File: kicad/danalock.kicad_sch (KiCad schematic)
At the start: 10 parts, among them J1 Conn_02x02_Top_Bottom, M1 Motor_DC, SW1 Rotary_Encoder, U1 WeMos_D1_mini, U2 HW-133, U3 TB6612FNG_Module

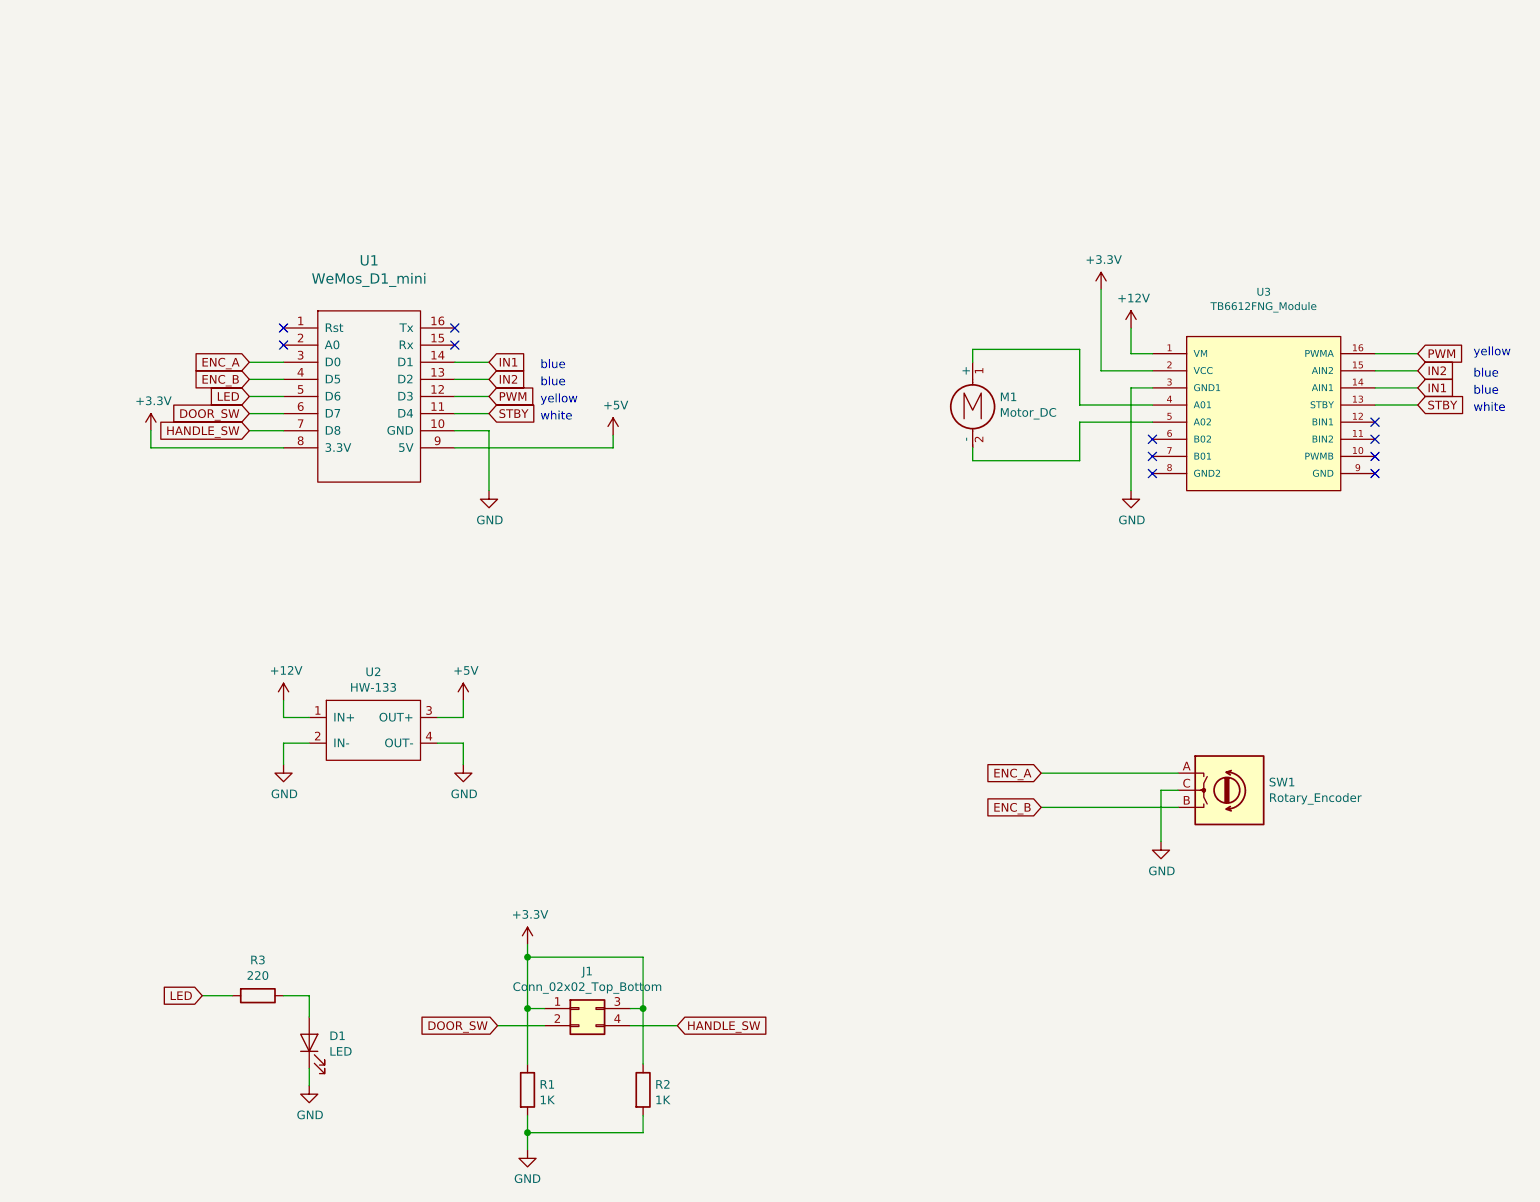
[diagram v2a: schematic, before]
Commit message: Port to ESP32.
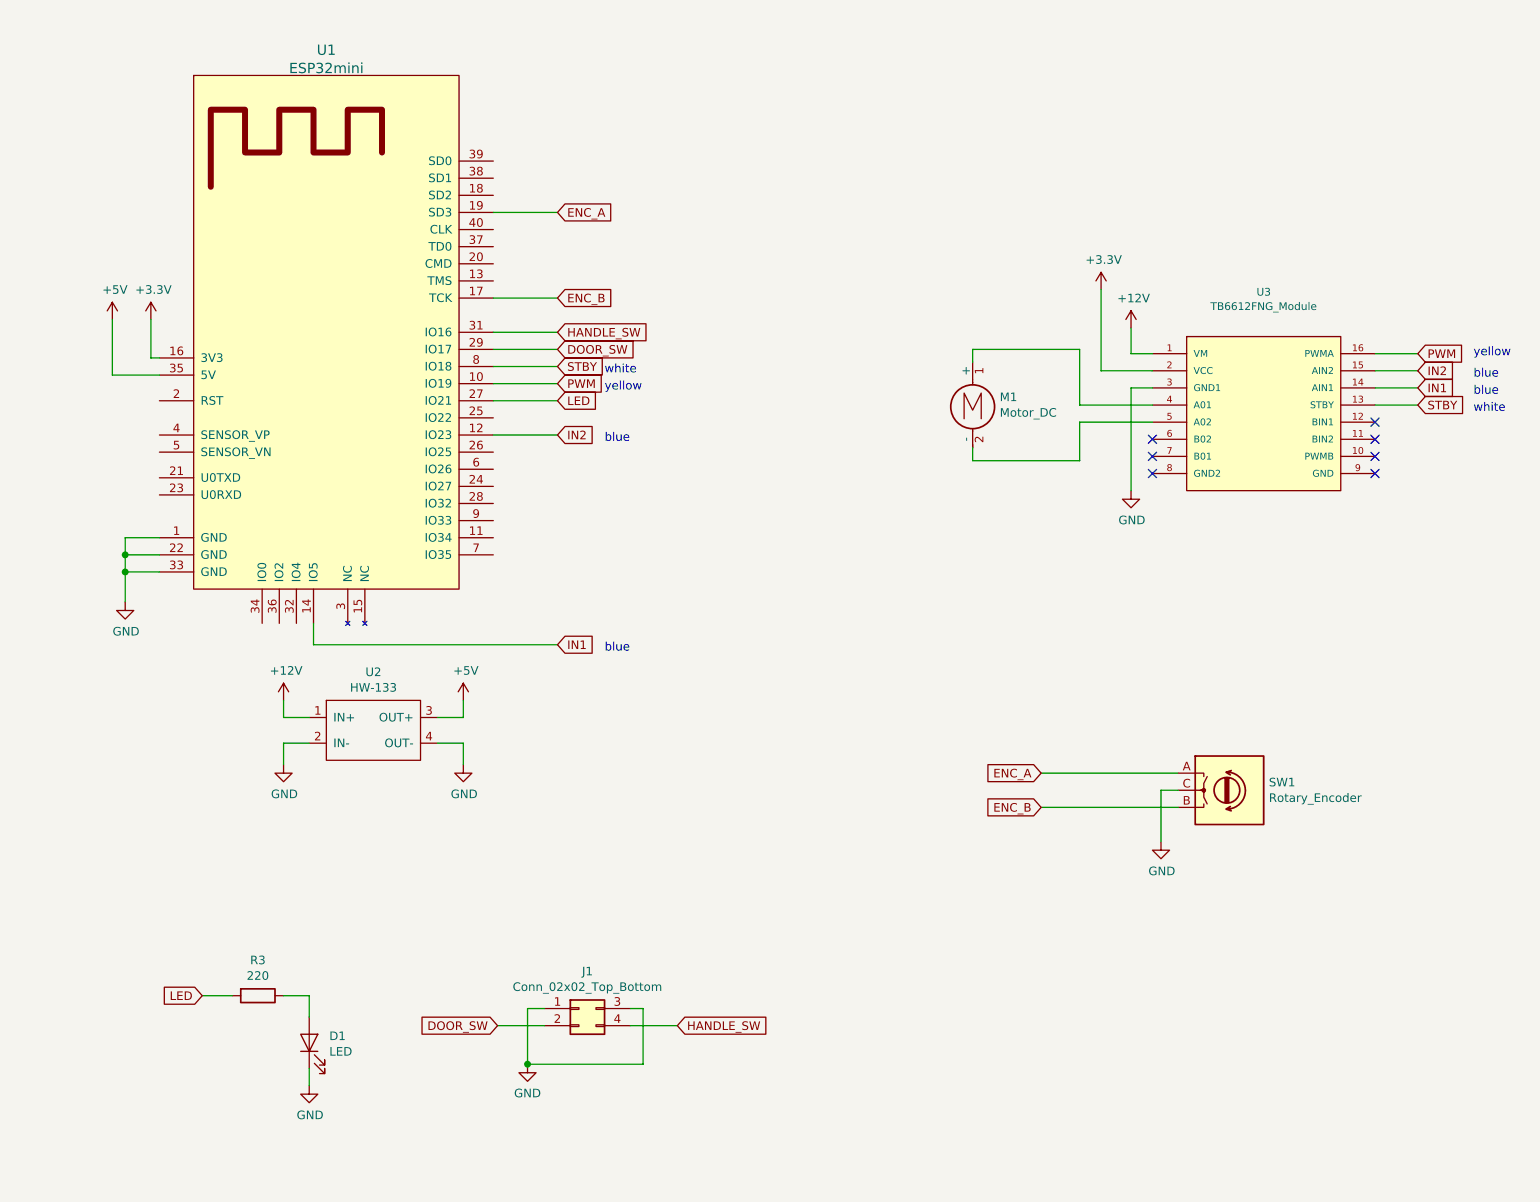
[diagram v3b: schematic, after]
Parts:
- removed R1, R2: 1K, symbol Device:R
- removed U1: WeMos_D1_mini, symbol wemos_mini:WeMos_D1_mini
- added U1: ESP32mini, ESP32mini:ESP32mini, symbol esp32mini:ESP32mini
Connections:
- net +3V3: now also U1.16 (3V3); no longer J1.1 (Pin_1), J1.3 (Pin_3)
- net +5V: now also U1.35 (5V)
- net DOOR_SW: now also U1.29 (IO17)
- net ENC_A: now also U1.19 (SD3)
- net ENC_B: now also U1.17 (TCK)
- net GND: now also J1.1 (Pin_1), J1.3 (Pin_3), U1.1 (GND), U1.22 (GND), U1.33 (GND)
- net HANDLE_SW: now also U1.31 (IO16)
- net IN1: now also U1.14 (IO5)
- net IN2: now also U1.12 (IO23)
- net LED: now also U1.27 (IO21)
- net PWM: now also U1.10 (IO19)
- net STBY: now also U1.8 (IO18)
- no-connect marks 11 -> 7

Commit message: Integrate motor driver and SMPS.
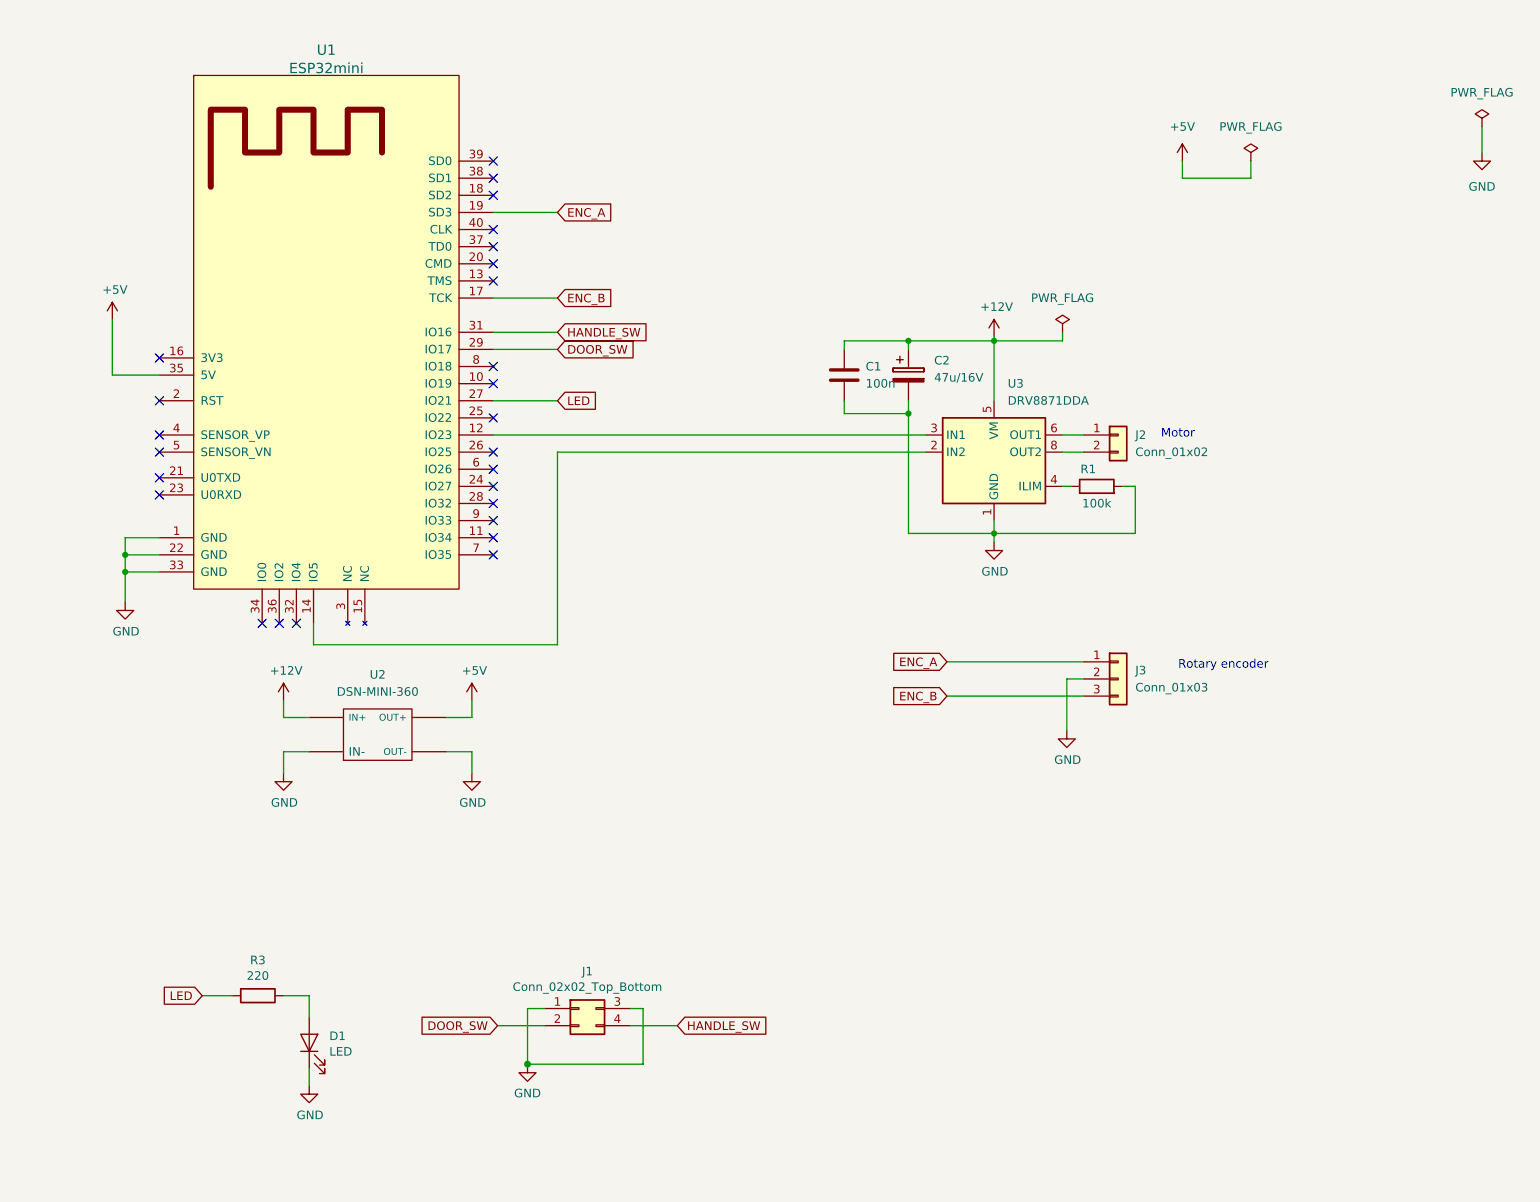
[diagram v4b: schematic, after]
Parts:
- removed M1: Motor_DC, symbol Motor:Motor_DC
- removed SW1: Rotary_Encoder, symbol Device:Rotary_Encoder
- removed U2: HW-133, mylib:buck-converter, symbol buck-converter:buck-converter
- removed U3: TB6612FNG_Module, SSOP24, symbol tb6612fng_module:TB6612FNG_Module
- added C1: 100n, symbol Device:C
- added C2: 47u/16V, symbol Device:CP
- added J2: Conn_01x02, symbol Connector_Generic:Conn_01x02
- added J3: Conn_01x03, symbol Connector_Generic:Conn_01x03
- added R1: 100k, symbol Device:R
- added U2: DSN-MINI-360, symbol dsnmini360:DSN-MINI-360
- added U3: DRV8871DDA, Package_SO:Texas_HTSOP-8-1EP_3.9x4.9mm_P1.27mm_EP2.95x4.9mm_Mask2.4x3.1mm_ThermalVias, symbol Driver_Motor:DRV8871DDA
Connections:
- net +12V: now also C1.1, C2.1, U2.IN+, U3.5 (VM)
- net +5V: now also U2.OUT+
- net ENC_A: now also J3.1 (Pin_1)
- net ENC_B: now also J3.3 (Pin_3)
- net GND: now also C1.2, C2.2, J3.2 (Pin_2), R1.2, U2.IN-, U2.OUT-, U3.1 (GND), U3.7 (GND), U3.9 (GND)
- net +3V3: no longer names the net of U1.16 (3V3)
- net IN1: no longer names the net of U1.14 (IO5)
- net IN1: now also U3.2 (IN2)
- net IN2: no longer names the net of U1.12 (IO23)
- net IN2: now also U3.3 (IN1)
- net PWM: no longer names the net of U1.10 (IO19)
- net STBY: no longer names the net of U1.8 (IO18)
- new net: J2.1 (Pin_1), U3.6 (OUT1)
- new net: J2.2 (Pin_2), U3.8 (OUT2)
- new net: R1.1, U3.4 (ILIM)
- no-connect marks 7 -> 26
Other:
- note added: "Motor"
- note added: "Rotary encoder"
- note removed: "blue"
- note removed: "white"
- note removed: "yellow"

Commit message: KiCAD update.
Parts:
- removed C2: 47u/16V, symbol Device:CP
- removed J1: Conn_02x02_Top_Bottom, symbol Connector_Generic:Conn_02x02_Top_Bottom
- removed J2: Conn_01x02, symbol Connector_Generic:Conn_01x02
- removed U1: ESP32mini, ESP32mini:ESP32mini, symbol esp32mini:ESP32mini
- removed U3: DRV8871DDA, Package_SO:Texas_HTSOP-8-1EP_3.9x4.9mm_P1.27mm_EP2.95x4.9mm_Mask2.4x3.1mm_ThermalVias, symbol Driver_Motor:DRV8871DDA
- added C2: 100n, Capacitor_SMD:C_0603_1608Metric, symbol Device:C
- added J1: Conn_01x02, Connector_JST:JST_XH_B2B-XH-A_1x02_P2.50mm_Vertical, symbol Connector_Generic:Conn_01x02
- added J2: Conn_01x07, Connector_PinSocket_2.00mm:PinSocket_1x07_P2.00mm_Vertical, symbol Connector_Generic:Conn_01x07
- added R2: 100, Resistor_SMD:R_0603_1608Metric, symbol Device:R
- added U1: ESP32mini_shield_inner, hal9k:ESP32mini_shield_inner, symbol esp32mini-shield-inner:ESP32mini_shield_inner
- C1: footprint (none) -> Capacitor_SMD:C_0603_1608Metric
- D1: footprint (none) -> LED_THT:LED_D5.0mm
- J3: footprint (none) -> Connector_PinSocket_2.00mm:PinSocket_1x03_P2.00mm_Vertical
- R1: value 100k -> 100; footprint (none) -> Resistor_SMD:R_0603_1608Metric
- R3: footprint (none) -> Resistor_SMD:R_0603_1608Metric
- U2: footprint (none) -> hal9k:DSN-MINI-360
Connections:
- net +12V: now also J1.1 (Pin_1); no longer C1.1
- net +5V: now also U1.35 (5V)
- net DOOR_SW: now also R1.1, C2.1, U1.29 (IO17)
- net ENC_A: now also J2.1 (Pin_1), U1.20 (SD3); no longer J3.1 (Pin_1)
- net ENC_B: now also J2.2 (Pin_2), U1.18 (TCK); no longer J3.3 (Pin_3)
- net GND: now also C2.2, J1.2 (Pin_2), J2.7 (Pin_7), U1.33 (GND); no longer R1.2
- net HANDLE_SW: now also C1.1, R2.1, U1.31 (IO16)
- net LED: now also U1.27 (IO21)
- new net: J3.1 (Pin_1), R1.2
- new net: J3.3 (Pin_3), R2.2
- new net IN1: J2.3 (Pin_3), U1.14 (IO5)
- new net IN2: J2.4 (Pin_4), U1.12 (IO23)
- new net PWM: J2.5 (Pin_5), U1.10 (IO19)
- new net STBY: J2.6 (Pin_6), U1.8 (IO18)
- no-connect marks 26 -> 9
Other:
- note added: "PWR IN"
- note added: "Switches"
